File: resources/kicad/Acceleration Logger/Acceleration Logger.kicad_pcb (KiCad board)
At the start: 2 copper layers, 42 x 58.1 mm, 12 parts, among them J1 Screw_Terminal_01x02, J2 USB_B_Micro, Q1 2N3904, U1 ESP8266-01s, U2 MPU6050, U3 MCP1700x-330xxTO

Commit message: Many updates
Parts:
- added R3: 1K, Resistor_SMD:R_0805_2012Metric_Pad1.20x1.40mm_HandSolder, F.Cu at (157.5, 115.7)
- moved C1 13.5 mm to (154.9, 85.6)
- moved R2 0.62 mm to (157.4, 119.5)
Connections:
- U1 pad 2: Net-(U1-U0TXD/GPIO1) -> Net-(D1-A)
- U1 pad 7: Net-(D1-A) -> Net-(U1-GPIO3/U0RXD)
- U2 pad 8: Net-(U1-U0TXD/GPIO1) -> Net-(U1-GPIO3/U0RXD)
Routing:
- net Net-(U1-GPIO3/U0RXD): track 0.00 -> 20.5 mm
- net Net-(U1-U0TXD/GPIO1): track 19.9 -> 0.00 mm
- net Net-(D1-A): track 46.7 -> 61.1 mm
- net /+5V: track 21.0 -> 12.9 mm
- net +3V3: track 85.0 -> 88.8 mm
- net Earth: track 125.9 -> 123.5 mm
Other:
- board text added: "+5V"
- board text added: "Acceleration Logger Ver 0.0.2 3/7/25 David E. Powell"
- board text added: "Gnd"
- board text removed: "Acceleration Logger 3/7/25 David E. Powell"

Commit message: Board updates
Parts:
- J1: value Screw_Terminal_01x02 -> Vehicle Brakes
- Q1: value 2N3904 -> IRLML6344
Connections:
- net Net-(DISP1-SDA) renamed /SDA
- J1 pad 1: +3V3 -> Net-(J1-Pin_1)
- J1 pad 2: Net-(J1-Pin_2) -> Earth
- Q1 pad 3: Net-(J1-Pin_2) -> Net-(J1-Pin_1)
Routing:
- net Earth: track 123.5 -> 142.3 mm
- net Net-(J1-Pin_1): track 0.00 -> 11.5 mm
- net Net-(J1-Pin_2): track 5.21 -> 0.00 mm
- net +3V3: track 88.8 -> 87.0 mm
- net Net-(Q1-B): track 18.3 -> 20.0 mm
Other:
- board text added: "+"
- board text added: "-"
- board text added: "Acceleration Logger Ver 0.1.0 4/7/25 David E. Powell"
- board text removed: "Acceleration Logger Ver 0.0.2 3/7/25 David E. Powell"

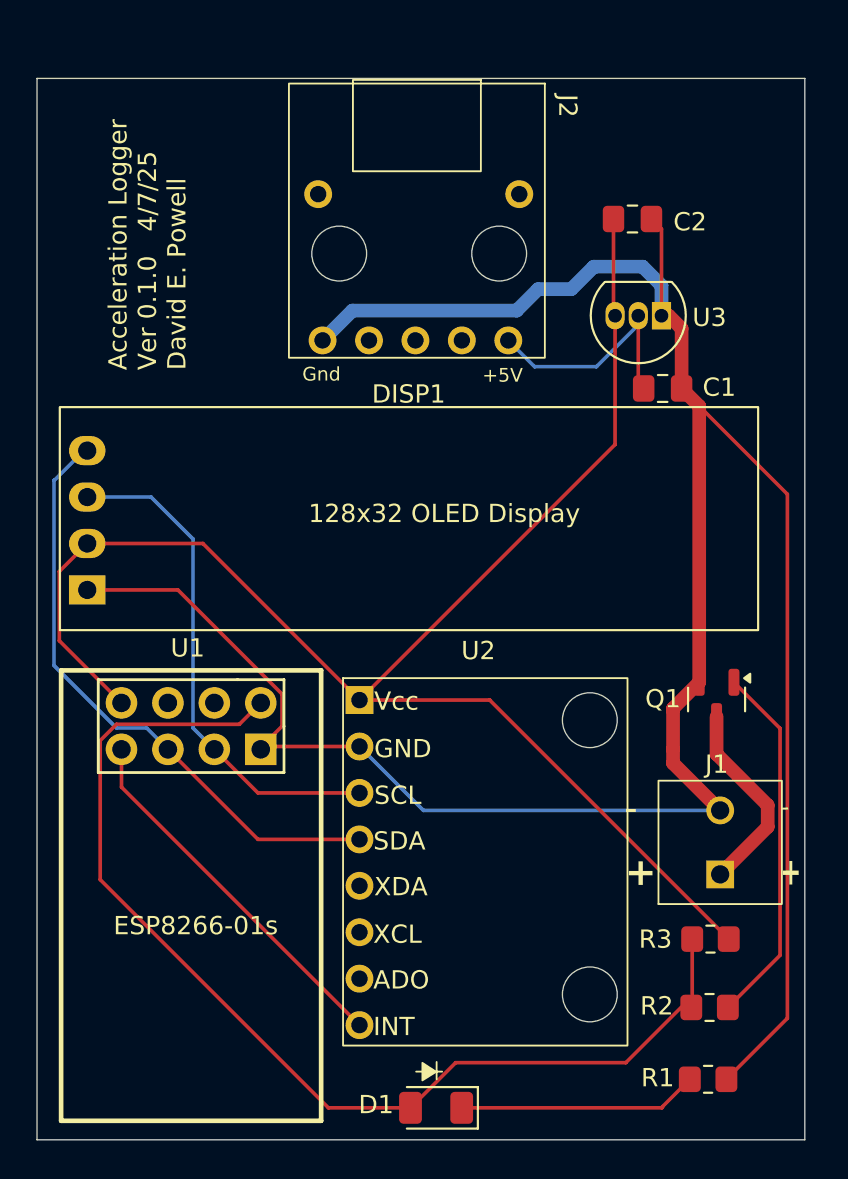
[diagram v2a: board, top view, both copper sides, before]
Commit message: Added "set level" feature. Changed LED to T1-3/4 size
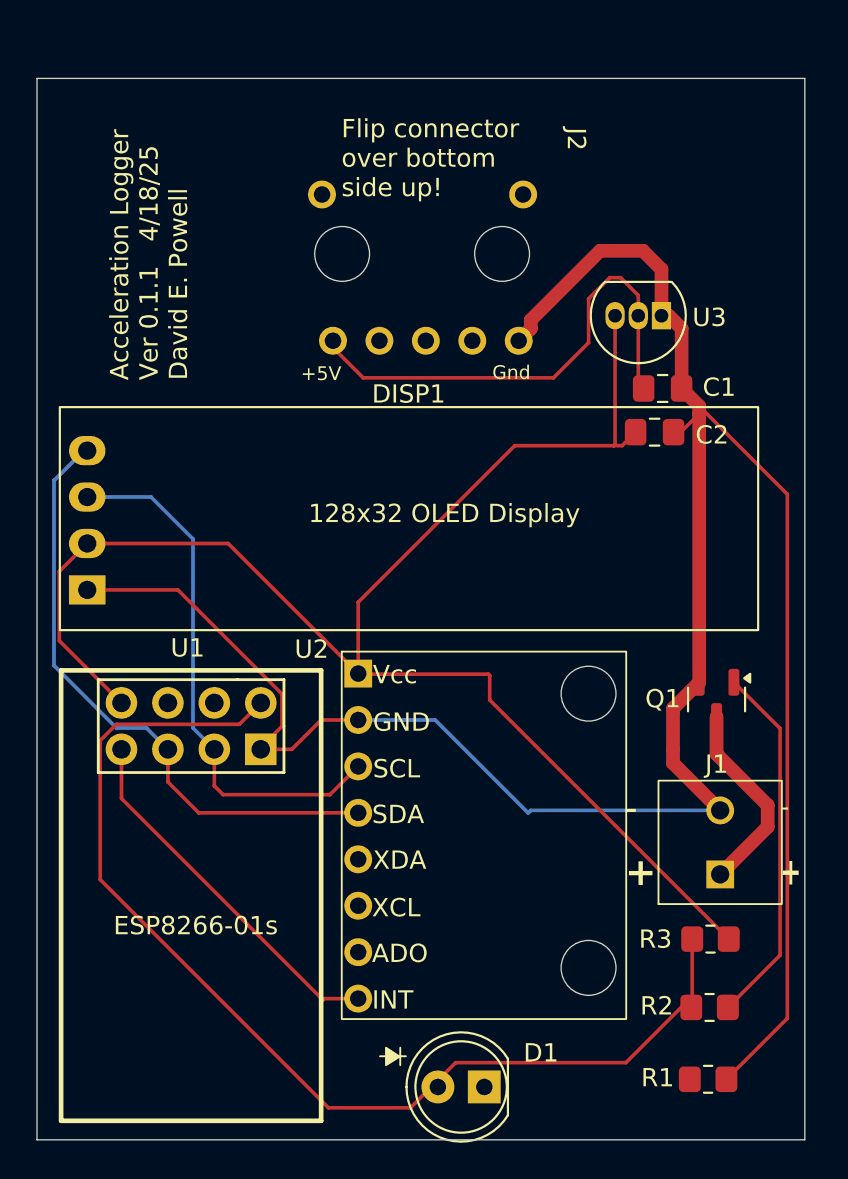
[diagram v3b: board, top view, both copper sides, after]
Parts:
- D1: footprint LED_SMD:LED_1206_3216Metric -> LED_THT:LED_D5.0mm
- J2: moved to B.Cu
- R2: value 1K -> 330
- R3: value 1K -> 10K
- moved C2 11.7 mm to (154.4, 88.0)
- moved J2 9.59 mm to (136.8, 83.0)
- moved D1 2.88 mm to (145.1, 123.8)
- moved U2 1.45 mm to (138.2, 101.2)
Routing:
- net /+5V: track 13.3 -> 27.4 mm
- net Net-(D1-K): track 13.1 -> 0.00 mm
- net Earth: track 142.3 -> 131.0 mm
- net Net-(DISP1-SCL): track 27.7 -> 29.4 mm
- net +3V3: track 87.0 -> 85.7 mm
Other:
- board text added: "Acceleration Logger Ver 0.1.1 4/18/25 David E. Powell"
- board text added: "Flip connector over bottom side up!"
- board text removed: "Acceleration Logger Ver 0.1.0 4/7/25 David E. Powell"
